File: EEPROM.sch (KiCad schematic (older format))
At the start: 10 parts

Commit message: Added EEPROM and LED circuits to schematic
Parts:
- removed D?: KP-1608CGCK, antmicro-footprints:LED_0603, symbol antmicroLEDIndicationDiscrete:KP-1608CGCK
- removed D?: LG_L29K-G2J1-24-Z, antmicro-footprints:LED_0603, symbol antmicroLEDIndicationDiscrete:LG_L29K-G2J1-24-Z
- removed D?: LH_R974-LP-1, antmicro-footprints:0805, symbol antmicroLEDIndicationDiscrete:LH_R974-LP-1
- removed D?: LTST-C150KRKT, antmicro-footprints:1206, symbol antmicroLEDIndicationDiscrete:LTST-C150KRKT
- added C? (x2): C_4u7_0402, lpddr4-testbed-footprints:0402-cap, symbol lpddr4-testbed:C_4u7_0402
- added C?: C_100n_0402, lpddr4-testbed-footprints:0402-cap, symbol lpddr4-testbed:C_100n_0402
- added D? (x4): KP-1608CGCK, lpddr4-testbed-footprints:LED_0603, symbol lpddr4-testbed:KP-1608CGCK
- added R?: R_0R_0402, lpddr4-testbed-footprints:0402-res, symbol lpddr4-testbed:R_0R_0402
- added R? (x4): R_220R_0402, lpddr4-testbed-footprints:0402-res, symbol lpddr4-testbed:R_220R_0402
- added R?: R_10k_0402, lpddr4-testbed-footprints:0402-res, symbol lpddr4-testbed:R_10k_0402
- added TP? (x3): TP_SMD1MM, lpddr4-testbed-footprints:Testpoint_smd_1mm, symbol lpddr4-testbed:TP_SMD1MM
- C?: footprint antmicro-footprints:0402-cap -> lpddr4-testbed-footprints:0402-cap; symbol antmicroCapacitors0402:C_100n_0402 -> lpddr4-testbed:C_100n_0402
- IC?: footprint antmicro-footprints:SOT-23-5 -> lpddr4-testbed-footprints:SOT-23-5; symbol antmicroMemory:AT24CS01 -> lpddr4-testbed:AT24CS01-antmicroMemory
- IC?: footprint antmicro-footprints:TSSOP-16 -> lpddr4-testbed-footprints:TSSOP-16; symbol antmicroInterfaceIOExpanders:PCA96408APW -> lpddr4-testbed:PCA96408APW-antmicroInterfaceIOExpanders
- L?: footprint antmicro-footprints:0805-res -> lpddr4-testbed-footprints:0805-res; symbol antmicroFixedInductors:1285AS-H-2R2M=P2 -> lpddr4-testbed:1285AS-H-2R2M=P2
- U?: footprint antmicro-footprints:SOT-23-5 -> lpddr4-testbed-footprints:SOT-23-5; symbol antmicroDCDCConverters:TPS613221ADBVT -> lpddr4-testbed:TPS613221ADBVT-antmicroDCDCConverters
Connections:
- net labels added: VDDLED
- net labels removed: VDDQ
- wire segments 22 -> 61
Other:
- note removed: "VDDQ"
- moved on the sheet: C?, IC?, L?, R?, U?

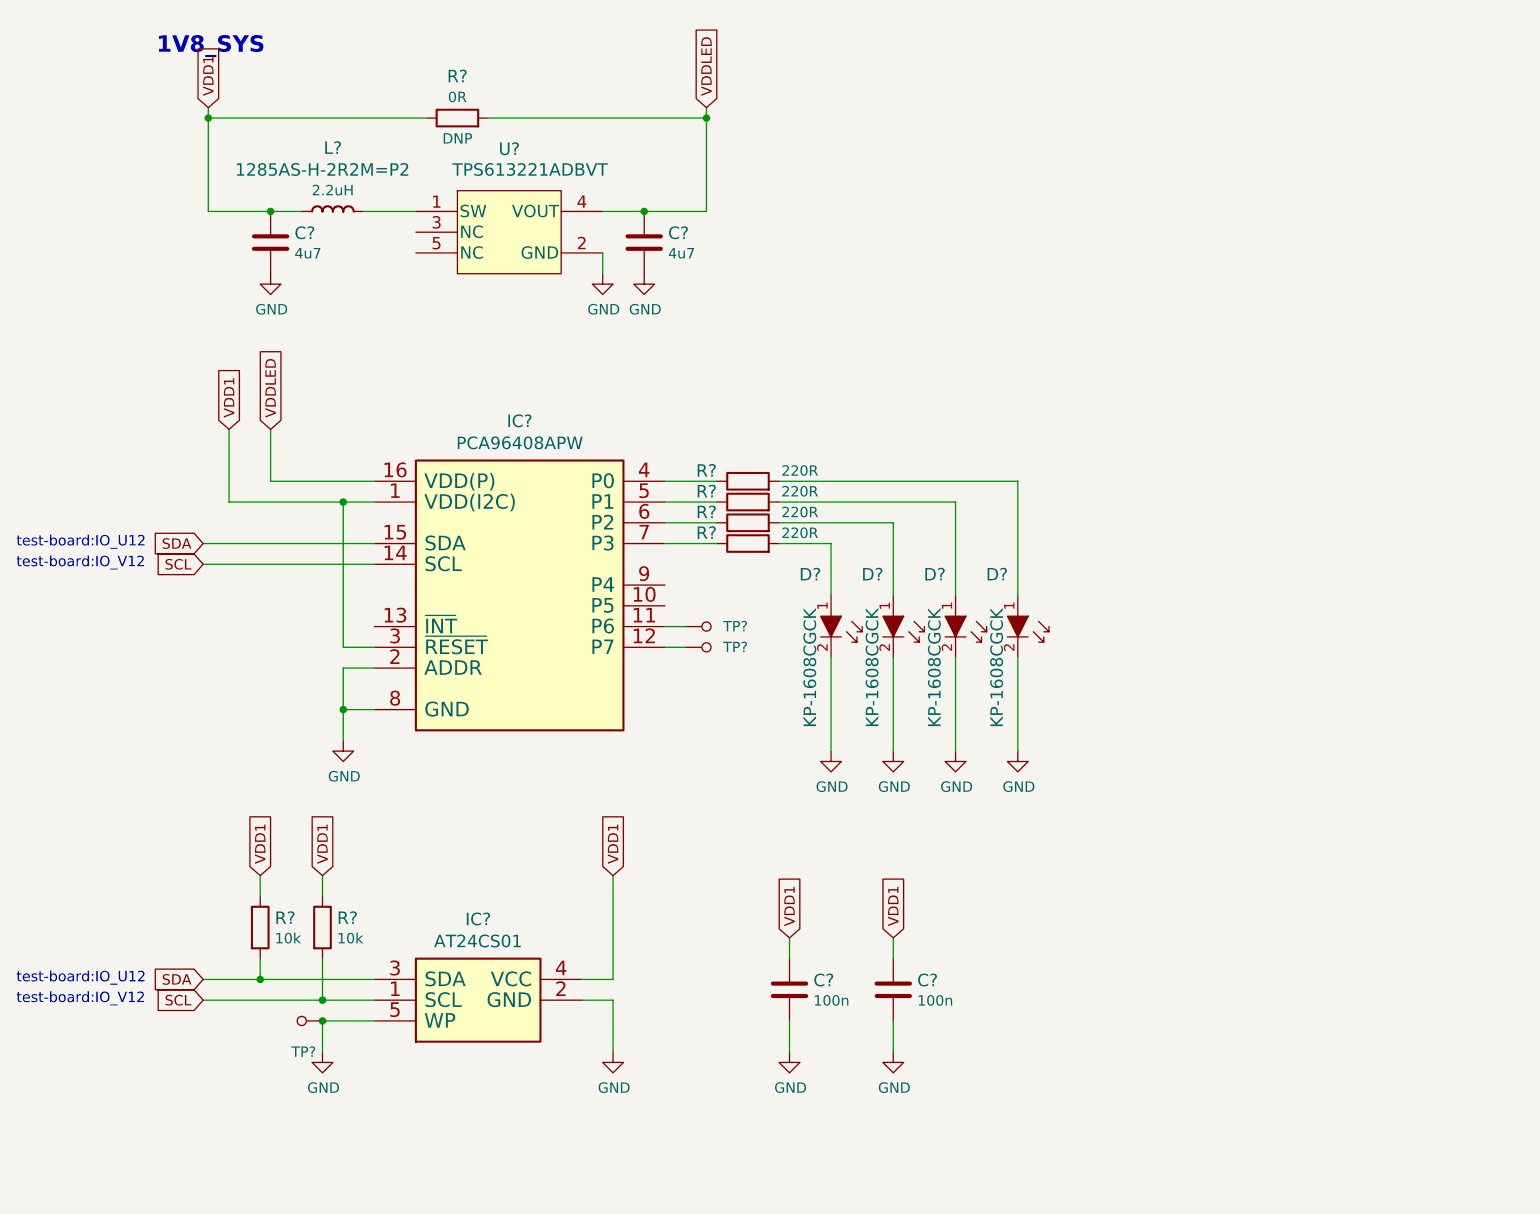
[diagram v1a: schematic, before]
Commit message: Component placement for EEPROM/LEDs
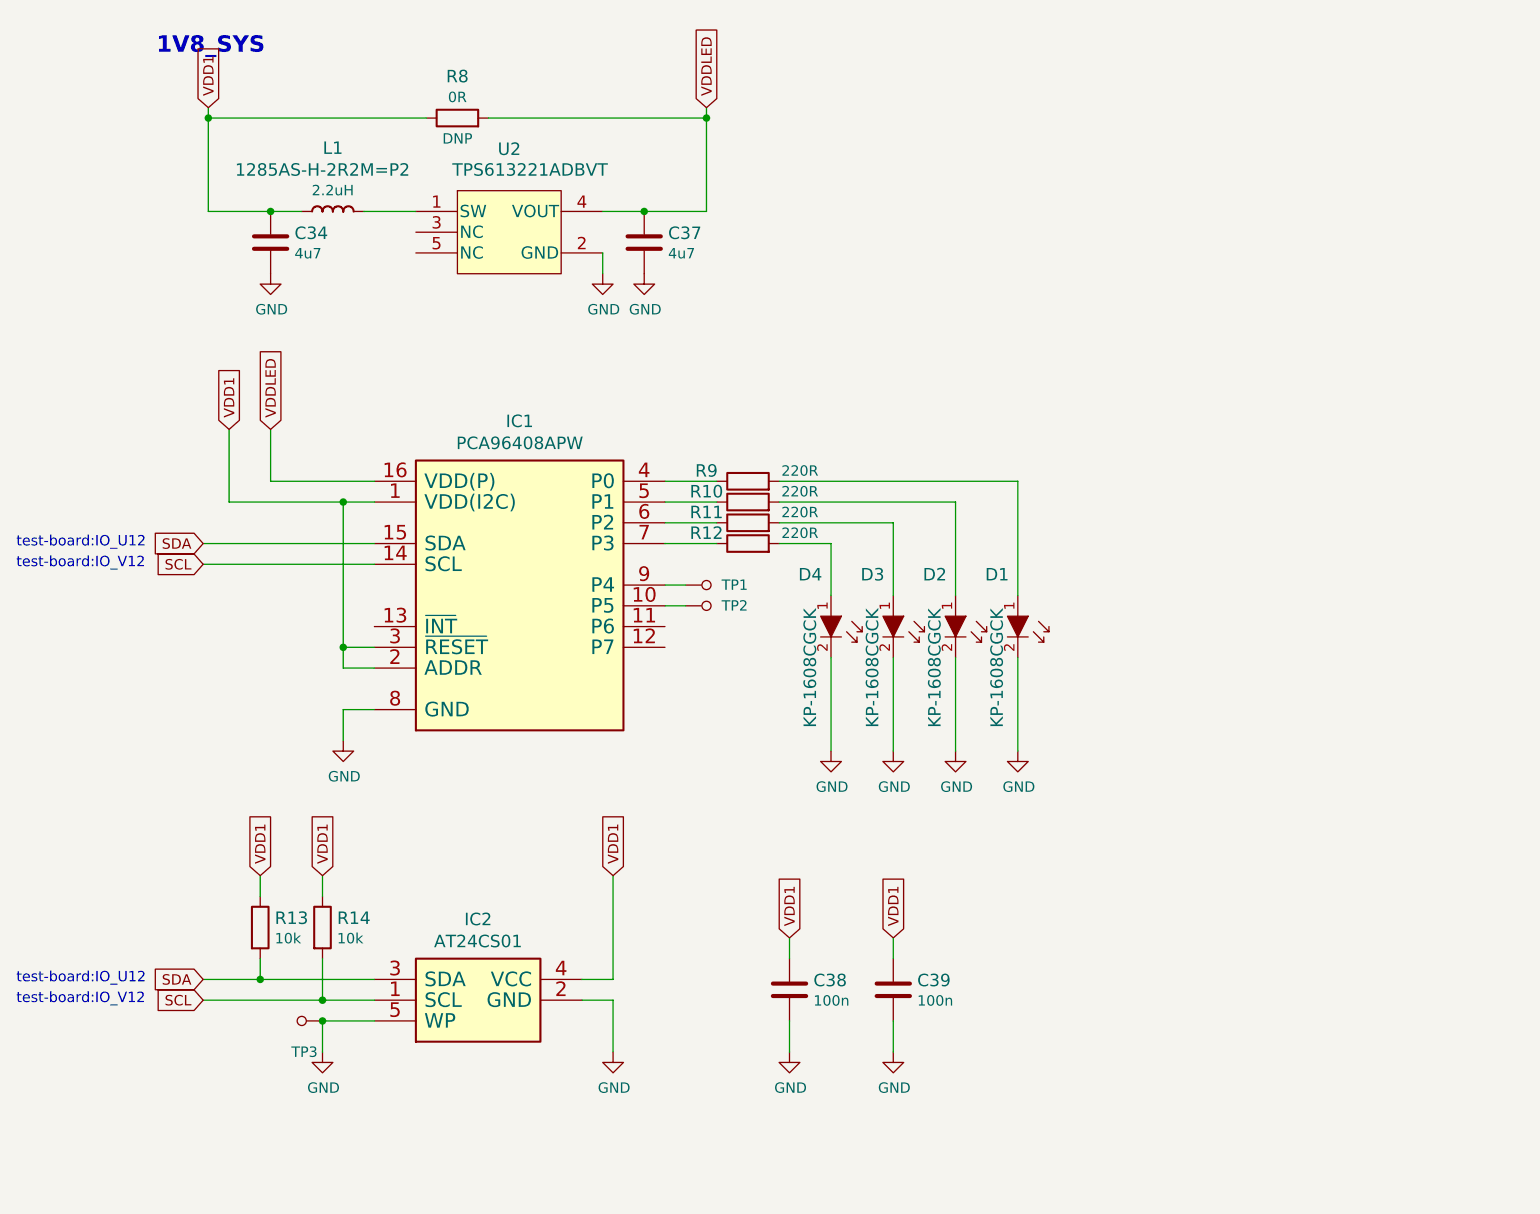
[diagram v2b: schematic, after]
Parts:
- gave numbers to parts that had none: 22
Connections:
- net GND: no longer IC1.2 (ADDR)
- net VDD1: now also IC1.2 (ADDR)
- net at IC1.10 (P5): now also TP2.1
- net at IC1.11 (P6): no longer TP1.1
- net at IC1.12 (P7): no longer TP2.1
- net at IC1.9 (P4): now also TP1.1
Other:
- moved on the sheet: TP1, TP2
